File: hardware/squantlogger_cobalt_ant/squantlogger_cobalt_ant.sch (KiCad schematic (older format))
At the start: 5 parts, among them J1 JTAG_2X05, M1 SUPERTRONIC37_51, M2 LPC824M201JHI33

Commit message: * updated cobalt ant datalogger PCB
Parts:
- removed M1: SUPERTRONIC37_51, SquantorPcbOutline:SUPERTRONIC_PP40, symbol SUPERTRONIC37_51
- added H1: Drill_Hole_no_metal, SquantorPcbOutline:MountingHole_2.2mm_no_metal, symbol Drill_Hole_no_metal
- added H2, H3: Drill_Hole_no_metal, SquantorPcbOutline:MountingHole_3.0mm_no_metal, symbol Drill_Hole_no_metal
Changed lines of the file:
@@
 $EndComp
 $Comp
-L GND #PWR01
+L GND #PWR2
 U 1 1 5921F82A
 P 2950 2200
-F 0 "#PWR01" H 2950 1950 50  0001 C CNN
+F 0 "#PWR2" H 2950 1950 50  0001 C CNN
 F 1 "GND" H 2950 2050 50  0000 C CNN
 F 2 "" H 2950 2200 50  0001 C CNN
@@
 $EndComp
 $Comp
-L VCC #PWR02
+L VCC #PWR1
 U 1 1 5921F856
 P 2950 1700
-F 0 "#PWR02" H 2950 1550 50  0001 C CNN
+F 0 "#PWR1" H 2950 1550 50  0001 C CNN
 F 1 "VCC" H 2950 1850 50  0000 C CNN
 F 2 "" H 2950 1700 50  0001 C CNN
@@
 	1900 2150 1150 2150
 $Comp
-L SUPERTRONIC37_51 M1
-U 1 1 5921FBE6
-P 2100 3550
-F 0 "M1" H 1700 3450 45  0000 L BNN
-F 1 "SUPERTRONIC37_51" H 1700 3250 45  0000 L BNN
-F 2 "SquantorPcbOutline:SUPERTRONIC_PP40" H 2130 3700 20  0001 C CNN
-F 3 "" H 2100 3550 60  0001 C CNN
-	1    2100 3550
-	1    0    0    -1
-$EndComp
-$Comp
-L GND #PWR03
+L GND #PWR3
 U 1 1 5921FF75
 P 8100 4100
-F 0 "#PWR03" H 8100 3850 50  0001 C CNN
+F 0 "#PWR3" H 8100 3850 50  0001 C CNN
 F 1 "GND" H 8100 3950 50  0000 C CNN
 F 2 "" H 8100 4100 50  0001 C CNN
@@
 $EndComp
 $Comp
-L VCC #PWR04
+L VCC #PWR6
 U 1 1 5921FFB7
 P 8950 3550
-F 0 "#PWR04" H 8950 3400 50  0001 C CNN
+F 0 "#PWR6" H 8950 3400 50  0001 C CNN
 F 1 "VCC" H 8950 3700 50  0000 C CNN
 F 2 "" H 8950 3550 50  0001 C CNN
@@
 	8800 3550 8950 3550
 $Comp
-L GND #PWR05
+L GND #PWR5
 U 1 1 59220010
 P 8950 3450
-F 0 "#PWR05" H 8950 3200 50  0001 C CNN
+F 0 "#PWR5" H 8950 3200 50  0001 C CNN
 F 1 "GND" H 8950 3300 50  0000 C CNN
 F 2 "" H 8950 3450 50  0001 C CNN
@@
 	8800 3450 8950 3450
 $Comp
-L VCC #PWR06
+L VCC #PWR4
 U 1 1 59220055
 P 8950 3350
-F 0 "#PWR06" H 8950 3200 50  0001 C CNN
+F 0 "#PWR4" H 8950 3200 50  0001 C CNN
 F 1 "VCC" H 8950 3500 50  0000 C CNN
 F 2 "" H 8950 3350 50  0001 C CNN
@@
 	2900 1950 2950 1950
 Connection ~ 2950 1950
+$Comp
+L Drill_Hole_no_metal H1
+U 1 1 592DD359
+P 1700 6350
+F 0 "H1" H 1700 6100 60  0000 C CNN
+F 1 "Drill_Hole_no_metal" H 1700 6600 60  0000 C CNN
+F 2 "SquantorPcbOutline:MountingHole_2.2mm_no_metal" H 1700 6350 60  0000 C CNN
+F 3 "" H 1700 6350 60  0001 C CNN
+	1    1700 6350
+	1    0    0    -1
+$EndComp
+$Comp
+L Drill_Hole_no_metal H2
+U 1 1 592DD3BE
+P 1700 6950
+F 0 "H2" H 1700 6700 60  0000 C CNN
+F 1 "Drill_Hole_no_metal" H 1700 7200 60  0000 C CNN
+F 2 "SquantorPcbOutline:MountingHole_3.0mm_no_metal" H 1700 6950 60  0000 C CNN
+F 3 "" H 1700 6950 60  0001 C CNN
+	1    1700 6950
+	1    0    0    -1
+$EndComp
+$Comp
+L Drill_Hole_no_metal H3
+U 1 1 592DD415
+P 1700 7550
+F 0 "H3" H 1700 7300 60  0000 C CNN
+F 1 "Drill_Hole_no_metal" H 1700 7800 60  0000 C CNN
+F 2 "SquantorPcbOutline:MountingHole_3.0mm_no_metal" H 1700 7550 60  0000 C CNN
+F 3 "" H 1700 7550 60  0001 C CNN
+	1    1700 7550
+	1    0    0    -1
+$EndComp
 $EndSCHEMATC

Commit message: * some small mods
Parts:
- added J? (x2): PINS_1X12, symbol PINS_1X12
- added M1: SUPERTRONIC37_51, SquantorPcbOutline:SUPERTRONIC_PP40_logger, symbol SUPERTRONIC37_51
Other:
- moved on the sheet: J1, R1, R2
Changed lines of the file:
@@
 L JTAG_2X05 J1
 U 1 1 5921F65D
-P 2400 1950
-F 0 "J1" H 2400 2300 60  0000 C CNN
-F 1 "JTAG_2X05" H 2400 1600 60  0000 C CNN
-F 2 "SquantorConnectors:Header-0127-2X05-SMD" H 2400 2100 60  0001 C CNN
-F 3 "" H 2400 2100 60  0001 C CNN
-	1    2400 1950
+P 2250 1100
+F 0 "J1" H 2250 1450 60  0000 C CNN
+F 1 "JTAG_2X05" H 2250 750 60  0000 C CNN
+F 2 "SquantorConnectors:Header-0127-2X05-SMD" H 2250 1250 60  0001 C CNN
+F 3 "" H 2250 1250 60  0001 C CNN
+	1    2250 1100
 	1    0    0    -1
 $EndComp
@@
 L R R2
 U 1 1 5921F706
-P 1650 1750
-F 0 "R2" V 1730 1750 50  0000 C CNN
-F 1 "33" V 1650 1750 50  0000 C CNN
-F 2 "SquantorRcl:R_0402_hand" V 1580 1750 50  0001 C CNN
-F 3 "" H 1650 1750 50  0001 C CNN
-	1    1650 1750
+P 1500 900
+F 0 "R2" V 1580 900 50  0000 C CNN
+F 1 "33" V 1500 900 50  0000 C CNN
+F 2 "SquantorRcl:R_0402_hand" V 1430 900 50  0001 C CNN
+F 3 "" H 1500 900 50  0001 C CNN
+	1    1500 900
 	0    1    1    0
 $EndComp
@@
 L R R1
 U 1 1 5921F77B
-P 1400 1850
-F 0 "R1" V 1480 1850 50  0000 C CNN
-F 1 "33" V 1400 1850 50  0000 C CNN
-F 2 "SquantorRcl:R_0402_hand" V 1330 1850 50  0001 C CNN
-F 3 "" H 1400 1850 50  0001 C CNN
-	1    1400 1850
+P 1250 1000
+F 0 "R1" V 1330 1000 50  0000 C CNN
+F 1 "33" V 1250 1000 50  0000 C CNN
+F 2 "SquantorRcl:R_0402_hand" V 1180 1000 50  0001 C CNN
+F 3 "" H 1250 1000 50  0001 C CNN
+	1    1250 1000
 	0    1    1    0
 $EndComp
@@
 L GND #PWR2
 U 1 1 5921F82A
-P 2950 2200
-F 0 "#PWR2" H 2950 1950 50  0001 C CNN
-F 1 "GND" H 2950 2050 50  0000 C CNN
-F 2 "" H 2950 2200 50  0001 C CNN
-F 3 "" H 2950 2200 50  0001 C CNN
-	1    2950 2200
+P 2800 1350
+F 0 "#PWR2" H 2800 1100 50  0001 C CNN
+F 1 "GND" H 2800 1200 50  0000 C CNN
+F 2 "" H 2800 1350 50  0001 C CNN
+F 3 "" H 2800 1350 50  0001 C CNN
+	1    2800 1350
 	1    0    0    -1
 $EndComp
@@
 L VCC #PWR1
 U 1 1 5921F856
-P 2950 1700
-F 0 "#PWR1" H 2950 1550 50  0001 C CNN
-F 1 "VCC" H 2950 1850 50  0000 C CNN
-F 2 "" H 2950 1700 50  0001 C CNN
-F 3 "" H 2950 1700 50  0001 C CNN
-	1    2950 1700
-	1    0    0    -1
-$EndComp
-Wire Wire Line
-	2900 1750 2950 1750
-Wire Wire Line
-	2950 1750 2950 1700
-Wire Wire Line
-	2900 2150 2950 2150
-Wire Wire Line
-	2950 1850 2950 2200
-Wire Wire Line
-	1900 1750 1800 1750
-Wire Wire Line
-	1900 1850 1550 1850
-Text GLabel 1150 1750 0    60   Input ~ 0
+P 2800 850
+F 0 "#PWR1" H 2800 700 50  0001 C CNN
+F 1 "VCC" H 2800 1000 50  0000 C CNN
+F 2 "" H 2800 850 50  0001 C CNN
+F 3 "" H 2800 850 50  0001 C CNN
+	1    2800 850
+	1    0    0    -1
+$EndComp
+Wire Wire Line
+	2750 900  2800 900
+Wire Wire Line
+	2800 900  2800 850
+Wire Wire Line
+	2750 1300 2800 1300
+Wire Wire Line
+	2800 1000 2800 1350
+Wire Wire Line
+	1750 900  1650 900
+Wire Wire Line
+	1750 1000 1400 1000
+Text GLabel 1000 900  0    60   Input ~ 0
 SWDIO
-Text GLabel 1150 1850 0    60   Input ~ 0
+Text GLabel 1000 1000 0    60   Input ~ 0
 SWDCLK
 Wire Wire Line
-	1500 1750 1150 1750
-Wire Wire Line
-	1250 1850 1150 1850
-Text GLabel 1150 2150 0    60   Input ~ 0
+	1350 900  1000 900
+Wire Wire Line
+	1100 1000 1000 1000
+Text GLabel 1000 1300 0    60   Input ~ 0
 nRESET
 Wire Wire Line
-	1900 2150 1150 2150
+	1750 1300 1000 1300
 $Comp
 L GND #PWR3
@@
 	7400 2650 7300 2650
 Wire Wire Line
-	2900 1850 2950 1850
-Connection ~ 2950 2150
-Wire Wire Line
-	2900 1950 2950 1950
-Connection ~ 2950 1950
+	2750 1000 2800 1000
+Connection ~ 2800 1300
+Wire Wire Line
+	2750 1100 2800 1100
+Connection ~ 2800 1100
 $Comp
 L Drill_Hole_no_metal H1
@@
 	1    0    0    -1
 $EndComp
+$Comp
+L SUPERTRONIC37_51 M1
+U 1 1 59386C4C
+P 4050 6750
+F 0 "M1" H 3650 6650 45  0000 L BNN
+F 1 "SUPERTRONIC37_51" H 3650 6450 45  0000 L BNN
+F 2 "SquantorPcbOutline:SUPERTRONIC_PP40_logger" H 4080 6900 20  0000 C CNN
+F 3 "" H 4050 6750 60  0001 C CNN
+	1    4050 6750
+	1    0    0    -1
+$EndComp
+$Comp
+L PINS_1X12 J?
+U 1 1 59386E63
+P 750 2300
+F 0 "J?" H 700 3000 60  0000 C CNN
+F 1 "PINS_1X12" H 750 1600 60  0000 C CNN
+F 2 "" H 750 2850 60  0001 C CNN
+F 3 "" H 750 2850 60  0001 C CNN
+	1    750  2300
+	1    0    0    -1
+$EndComp
+$Comp
+L PINS_1X12 J?
+U 1 1 59386ED0
+P 750 3800
+F 0 "J?" H 700 4500 60  0000 C CNN
+F 1 "PINS_1X12" H 750 3100 60  0000 C CNN
+F 2 "" H 750 4350 60  0001 C CNN
+F 3 "" H 750 4350 60  0001 C CNN
+	1    750  3800
+	1    0    0    -1
+$EndComp

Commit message: * added few tidbits
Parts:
- added C? (x2): 10u, SquantorRcl:C_0805, symbol C
- H2, H3: footprint SquantorPcbOutline:MountingHole_3.0mm_no_metal -> SquantorPcbOutline:MountingHole_3.2mm_no_metal
- gave numbers to parts that had none: 2
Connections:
- net labels added: GNDA, VDD, VDDA
- wire segments 18 -> 22
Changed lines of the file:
@@
 LIBS:contrib
 LIBS:valves
+LIBS:SquantorPCBOutline
+LIBS:SquantorRCL
+LIBS:SquantorConnectors
 LIBS:SquantorButtons
-LIBS:SquantorConnectors
 LIBS:SquantorNxp
-LIBS:SquantorUsb
-LIBS:SquantorWinbond
-LIBS:SquantorAtmel
-LIBS:SquantorPCBOutline
 LIBS:squantlogger_cobalt_ant-cache
 EELAYER 25 0
@@
 $EndComp
 $Comp
-L GND #PWR2
+L GND #PWR6
 U 1 1 5921F82A
 P 2800 1350
-F 0 "#PWR2" H 2800 1100 50  0001 C CNN
+F 0 "#PWR6" H 2800 1100 50  0001 C CNN
 F 1 "GND" H 2800 1200 50  0000 C CNN
 F 2 "" H 2800 1350 50  0001 C CNN
@@
 $EndComp
 $Comp
-L VCC #PWR1
+L VCC #PWR5
 U 1 1 5921F856
 P 2800 850
-F 0 "#PWR1" H 2800 700 50  0001 C CNN
+F 0 "#PWR5" H 2800 700 50  0001 C CNN
 F 1 "VCC" H 2800 1000 50  0000 C CNN
 F 2 "" H 2800 850 50  0001 C CNN
@@
 	1750 1300 1000 1300
 $Comp
-L GND #PWR3
+L GND #PWR7
 U 1 1 5921FF75
 P 8100 4100
-F 0 "#PWR3" H 8100 3850 50  0001 C CNN
+F 0 "#PWR7" H 8100 3850 50  0001 C CNN
 F 1 "GND" H 8100 3950 50  0000 C CNN
 F 2 "" H 8100 4100 50  0001 C CNN
@@
 	1    0    0    -1
 $EndComp
-$Comp
-L VCC #PWR6
-U 1 1 5921FFB7
-P 8950 3550
-F 0 "#PWR6" H 8950 3400 50  0001 C CNN
-F 1 "VCC" H 8950 3700 50  0000 C CNN
-F 2 "" H 8950 3550 50  0001 C CNN
-F 3 "" H 8950 3550 50  0001 C CNN
-	1    8950 3550
-	0    1    1    0
-$EndComp
 Wire Wire Line
 	8100 4100 8100 3950
 Wire Wire Line
 	8800 3550 8950 3550
-$Comp
-L GND #PWR5
-U 1 1 59220010
-P 8950 3450
-F 0 "#PWR5" H 8950 3200 50  0001 C CNN
-F 1 "GND" H 8950 3300 50  0000 C CNN
-F 2 "" H 8950 3450 50  0001 C CNN
-F 3 "" H 8950 3450 50  0001 C CNN
-	1    8950 3450
-	0    -1   -1   0
-$EndComp
 Wire Wire Line
 	8800 3450 8950 3450
-$Comp
-L VCC #PWR4
-U 1 1 59220055
-P 8950 3350
-F 0 "#PWR4" H 8950 3200 50  0001 C CNN
-F 1 "VCC" H 8950 3500 50  0000 C CNN
-F 2 "" H 8950 3350 50  0001 C CNN
-F 3 "" H 8950 3350 50  0001 C CNN
-	1    8950 3350
-	0    1    1    0
-$EndComp
 Wire Wire Line
 	8800 3350 8950 3350
@@
 F 0 "H2" H 1700 6700 60  0000 C CNN
 F 1 "Drill_Hole_no_metal" H 1700 7200 60  0000 C CNN
-F 2 "SquantorPcbOutline:MountingHole_3.0mm_no_metal" H 1700 6950 60  0000 C CNN
+F 2 "SquantorPcbOutline:MountingHole_3.2mm_no_metal" H 1700 6950 60  0000 C CNN
 F 3 "" H 1700 6950 60  0001 C CNN
 	1    1700 6950
@@
 F 0 "H3" H 1700 7300 60  0000 C CNN
 F 1 "Drill_Hole_no_metal" H 1700 7800 60  0000 C CNN
-F 2 "SquantorPcbOutline:MountingHole_3.0mm_no_metal" H 1700 7550 60  0000 C CNN
+F 2 "SquantorPcbOutline:MountingHole_3.2mm_no_metal" H 1700 7550 60  0000 C CNN
 F 3 "" H 1700 7550 60  0001 C CNN
 	1    1700 7550
@@
 L SUPERTRONIC37_51 M1
 U 1 1 59386C4C
-P 4050 6750
-F 0 "M1" H 3650 6650 45  0000 L BNN
-F 1 "SUPERTRONIC37_51" H 3650 6450 45  0000 L BNN
-F 2 "SquantorPcbOutline:SUPERTRONIC_PP40_logger" H 4080 6900 20  0000 C CNN
-F 3 "" H 4050 6750 60  0001 C CNN
-	1    4050 6750
-	1    0    0    -1
-$EndComp
-$Comp
-L PINS_1X12 J?
+P 6200 7150
+F 0 "M1" H 5800 7050 45  0000 L BNN
+F 1 "SUPERTRONIC37_51" H 5800 6850 45  0000 L BNN
+F 2 "SquantorPcbOutline:SUPERTRONIC_PP40_logger" H 6230 7300 20  0000 C CNN
+F 3 "" H 6200 7150 60  0001 C CNN
+	1    6200 7150
+	1    0    0    -1
+$EndComp
+$Comp
+L PINS_1X12 J2
 U 1 1 59386E63
 P 750 2300
-F 0 "J?" H 700 3000 60  0000 C CNN
+F 0 "J2" H 700 3000 60  0000 C CNN
 F 1 "PINS_1X12" H 750 1600 60  0000 C CNN
 F 2 "" H 750 2850 60  0001 C CNN
@@
 $EndComp
 $Comp
-L PINS_1X12 J?
+L PINS_1X12 J3
 U 1 1 59386ED0
 P 750 3800
-F 0 "J?" H 700 4500 60  0000 C CNN
+F 0 "J3" H 700 4500 60  0000 C CNN
 F 1 "PINS_1X12" H 750 3100 60  0000 C CNN
 F 2 "" H 750 4350 60  0001 C CNN
@@
 	1    0    0    -1
 $EndComp
+$Comp
+L GNDA #PWR2
+U 1 1 5939A617
+P 800 5350
+F 0 "#PWR2" H 800 5100 50  0001 C CNN
+F 1 "GNDA" H 800 5200 50  0000 C CNN
+F 2 "" H 800 5350 50  0001 C CNN
+F 3 "" H 800 5350 50  0001 C CNN
+	1    800  5350
+	1    0    0    -1
+$EndComp
+$Comp
+L GND #PWR4
+U 1 1 5939A647
+P 1050 5350
+F 0 "#PWR4" H 1050 5100 50  0001 C CNN
+F 1 "GND" H 1050 5200 50  0000 C CNN
+F 2 "" H 1050 5350 50  0001 C CNN
+F 3 "" H 1050 5350 50  0001 C CNN
+	1    1050 5350
+	1    0    0    -1
+$EndComp
+$Comp
+L GNDA #PWR9
+U 1 1 5939A7EA
+P 8950 3450
+F 0 "#PWR9" H 8950 3200 50  0001 C CNN
+F 1 "GNDA" H 8950 3300 50  0000 C CNN
+F 2 "" H 8950 3450 50  0001 C CNN
+F 3 "" H 8950 3450 50  0001 C CNN
+	1    8950 3450
+	0    -1   -1   0
+$EndComp
+$Comp
+L VDD #PWR10
+U 1 1 5939A870
+P 8950 3550
+F 0 "#PWR10" H 8950 3400 50  0001 C CNN
+F 1 "VDD" H 8950 3700 50  0000 C CNN
+F 2 "" H 8950 3550 50  0001 C CNN
+F 3 "" H 8950 3550 50  0001 C CNN
+	1    8950 3550
+	0    1    1    0
+$EndComp
+$Comp
+L VDDA #PWR8
+U 1 1 5939A898
+P 8950 3350
+F 0 "#PWR8" H 8950 3200 50  0001 C CNN
+F 1 "VDDA" H 8950 3500 50  0000 C CNN
+F 2 "" H 8950 3350 50  0001 C CNN
+F 3 "" H 8950 3350 50  0001 C CNN
+	1    8950 3350
+	0    1    1    0
+$EndComp
+$Comp
+L VDD #PWR3
+U 1 1 5939AA02
+P 1050 4950
+F 0 "#PWR3" H 1050 4800 50  0001 C CNN
+F 1 "VDD" H 1050 5100 50  0000 C CNN
+F 2 "" H 1050 4950 50  0001 C CNN
+F 3 "" H 1050 4950 50  0001 C CNN
+	1    1050 4950
+	1    0    0    -1
+$EndComp
+$Comp
+L VDDA #PWR1
+U 1 1 5939AA2B
+P 800 4950
+F 0 "#PWR1" H 800 4800 50  0001 C CNN
+F 1 "VDDA" H 800 5100 50  0000 C CNN
+F 2 "" H 800 4950 50  0001 C CNN
+F 3 "" H 800 4950 50  0001 C CNN
+	1    800  4950
+	1    0    0    -1
+$EndComp
+$Comp
+L C C?
+U 1 1 5939A5DB
+P 800 5150
+F 0 "C?" H 825 5250 50  0000 L CNN
+F 1 "10u" H 825 5050 50  0000 L CNN
+F 2 "SquantorRcl:C_0805" H 838 5000 50  0001 C CNN
+F 3 "" H 800 5150 50  0001 C CNN
+	1    800  5150
+	1    0    0    -1
+$EndComp
+$Comp
+L C C?
+U 1 1 5939A905
+P 1050 5150
+F 0 "C?" H 1075 5250 50  0000 L CNN
+F 1 "10u" H 1075 5050 50  0000 L CNN
+F 2 "SquantorRcl:C_0805" H 1088 5000 50  0001 C CNN
+F 3 "" H 1050 5150 50  0001 C CNN
+	1    1050 5150
+	1    0    0    -1
+$EndComp
+Wire Wire Line
+	800  5000 800  4950
+Wire Wire Line
+	800  5300 800  5350
+Wire Wire Line
+	1050 5350 1050 5300
+Wire Wire Line
+	1050 5000 1050 4950
 $EndSCHEMATC

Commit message: * some further work on the cobalt ant datalogger
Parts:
- removed M1: SUPERTRONIC37_51, SquantorPcbOutline:SUPERTRONIC_PP40_logger, symbol SUPERTRONIC37_51
- removed M2: LPC824M201JHI33, SquantorNxp:SOT617-3, symbol LPC824M201JHI33
- added C3: 1u, SquantorRcl:C_0805, symbol C
- added C4, C6: 10n, SquantorRcl:C_0402, symbol C
- added C5, C7: 1u, SquantorRcl:C_0402, symbol C
- added J4: PINS_1X06, SquantorConnectors:Header-0254-1X06-H010, symbol PINS_1X06
- added M1: LPC824M201JDH20, SquantorNxp:SOT360, symbol LPC824M201JDH20
- added R3, R4, R5, R6: 100, SquantorRcl:R_0402_hand, symbol R
- added R7, R8: 10k, SquantorRcl:R_0402_hand, symbol R
- added U1: MCP1702-MB, SquantorMicrochip:MB-(SOT-89), symbol MCP1702-MB
- J2, J3: footprint (none) -> SquantorConnectors:Header-0254-1X12-H010
- gave numbers to parts that had none: 2
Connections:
- net labels added: +BATT, SERIAL_CTS, SERIAL_RTS, SERIAL_RXD, SERIAL_TXD
- net labels removed: VCC
- wire segments 22 -> 52
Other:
- moved on the sheet: C1, C2

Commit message: * started fleshing out the schematic of the squantlogger
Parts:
- removed J4: PINS_1X06, SquantorConnectors:Header-0254-1X06-H010, symbol PINS_1X06
- removed M1: LPC824M201JDH20, SquantorNxp:SOT360, symbol LPC824M201JDH20
- added 2.2k (x2): R, SquantorRcl:R_0402_hand, symbol R
- added J?: FTDI_PINS_1X06, symbol FTDI_PINS_1X06
- added M?: LPC824M201JHI33, SquantorNxp_SOT617-3, symbol LPC824M201JHI33
- added R? (x2): OPT, symbol R
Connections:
- net labels added: ADC_0, ADC_1, ADC_2, ADC_3, ADC_4, ADC_5, ADC_6, ADC_7, ADC_8, I2C_SCL, I2C_SDA, VREF
- wire segments 52 -> 82
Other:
- moved on the sheet: C4, C5, C6, C7

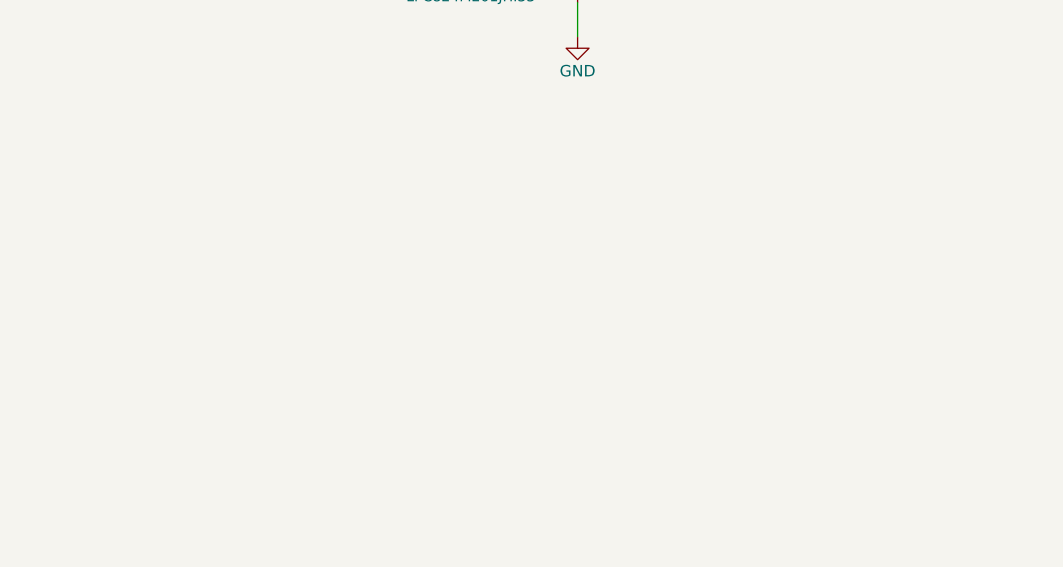
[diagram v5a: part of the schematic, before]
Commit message: * added spi flash to schematic
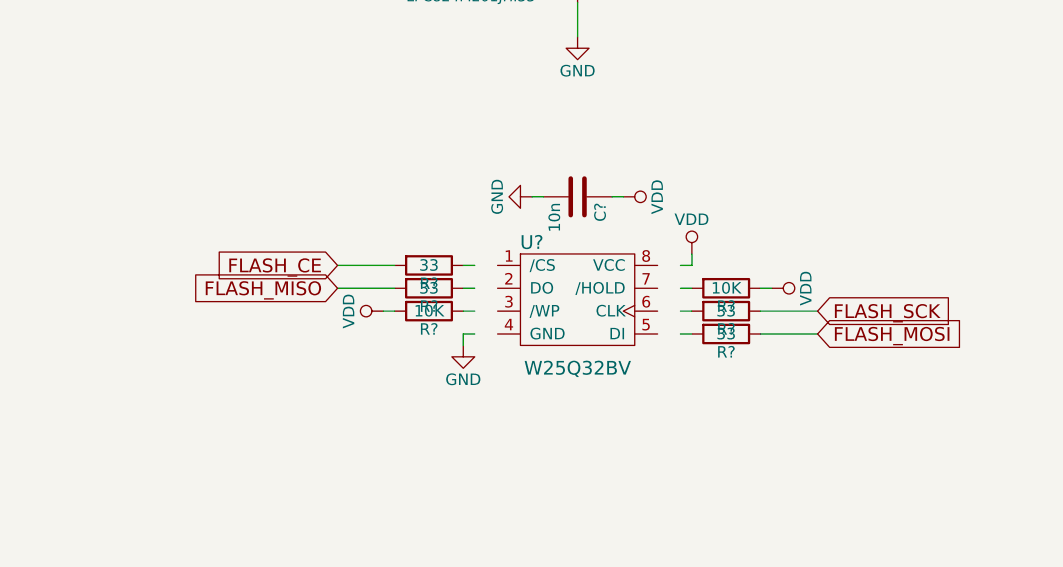
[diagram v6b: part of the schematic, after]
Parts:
- added C?: 10n, SquantorRcl:C_0402, symbol C
- added R? (x4): 33, SquantorRcl:R_0402_hand, symbol R
- added R? (x2): 10K, SquantorRcl:R_0402_hand, symbol R
- added U?: W25Q32BV, symbol W25Q32BV
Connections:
- net labels added: FLASH_CE, FLASH_MISO, FLASH_MOSI, FLASH_SCK
- wire segments 82 -> 100
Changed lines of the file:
@@
 LIBS:SquantorNxp
 LIBS:SquantorMicrochip
+LIBS:SquantorWinbond
 LIBS:squantlogger_cobalt_ant-cache
 EELAYER 25 0
@@
 Wire Wire Line
 	1000 4350 950  4350
+$Comp
+L W25Q32BV U?
+U 1 1 595545DA
+P 9200 4550
+F 0 "U?" H 9000 4800 60  0000 C CNN
+F 1 "W25Q32BV" H 9200 4250 60  0000 C CNN
+F 2 "" H 9150 4550 60  0001 C CNN
+F 3 "" H 9150 4550 60  0001 C CNN
+	1    9200 4550
+	1    0    0    -1
+$EndComp
+Text GLabel 8150 4400 0    60   Input ~ 0
+FLASH_CE
+$Comp
+L R R?
+U 1 1 59554929
+P 8550 4400
+F 0 "R?" V 8630 4400 50  0000 C CNN
+F 1 "33" V 8550 4400 50  0000 C CNN
+F 2 "SquantorRcl:R_0402_hand" V 8480 4400 50  0001 C CNN
+F 3 "" H 8550 4400 50  0001 C CNN
+	1    8550 4400
+	0    1    1    0
+$EndComp
+$Comp
+L R R?
+U 1 1 5955498E
+P 8550 4500
+F 0 "R?" V 8630 4500 50  0000 C CNN
+F 1 "33" V 8550 4500 50  0000 C CNN
+F 2 "SquantorRcl:R_0402_hand" V 8480 4500 50  0001 C CNN
+F 3 "" H 8550 4500 50  0001 C CNN
+	1    8550 4500
+	0    1    1    0
+$EndComp
+$Comp
+L R R?
+U 1 1 595549FD
+P 8550 4600
+F 0 "R?" V 8630 4600 50  0000 C CNN
+F 1 "10K" V 8550 4600 50  0000 C CNN
+F 2 "SquantorRcl:R_0402_hand" V 8480 4600 50  0001 C CNN
+F 3 "" H 8550 4600 50  0001 C CNN
+	1    8550 4600
+	0    1    1    0
+$EndComp
+$Comp
+L GND #PWR?
+U 1 1 59554BC2
+P 8700 4750
+F 0 "#PWR?" H 8700 4500 50  0001 C CNN
+F 1 "GND" H 8700 4600 50  0000 C CNN
+F 2 "" H 8700 4750 50  0001 C CNN
+F 3 "" H 8700 4750 50  0001 C CNN
+	1    8700 4750
+	1    0    0    -1
+$EndComp
+$Comp
+L VDD #PWR?
+U 1 1 59554E4D
+P 9700 4350
+F 0 "#PWR?" H 9700 4200 50  0001 C CNN
+F 1 "VDD" H 9700 4500 50  0000 C CNN
+F 2 "" H 9700 4350 50  0001 C CNN
+F 3 "" H 9700 4350 50  0001 C CNN
+	1    9700 4350
+	1    0    0    -1
+$EndComp
+Wire Wire Line
+	8700 4750 8700 4700
+Wire Wire Line
+	8700 4700 8750 4700
+Wire Wire Line
+	9700 4350 9700 4400
+Wire Wire Line
+	9700 4400 9650 4400
+$Comp
+L R R?
+U 1 1 59555150
+P 9850 4500
+F 0 "R?" V 9930 4500 50  0000 C CNN
+F 1 "10K" V 9850 4500 50  0000 C CNN
+F 2 "SquantorRcl:R_0402_hand" V 9780 4500 50  0001 C CNN
+F 3 "" H 9850 4500 50  0001 C CNN
+	1    9850 4500
+	0    1    1    0
+$EndComp
+$Comp
+L R R?
+U 1 1 595551BF
+P 9850 4600
+F 0 "R?" V 9930 4600 50  0000 C CNN
+F 1 "33" V 9850 4600 50  0000 C CNN
+F 2 "SquantorRcl:R_0402_hand" V 9780 4600 50  0001 C CNN
+F 3 "" H 9850 4600 50  0001 C CNN
+	1    9850 4600
+	0    1    1    0
+$EndComp
+$Comp
+L R R?
+U 1 1 5955521E
+P 9850 4700
+F 0 "R?" V 9930 4700 50  0000 C CNN
+F 1 "33" V 9850 4700 50  0000 C CNN
+F 2 "SquantorRcl:R_0402_hand" V 9780 4700 50  0001 C CNN
+F 3 "" H 9850 4700 50  0001 C CNN
+	1    9850 4700
+	0    1    1    0
+$EndComp
+$Comp
+L VDD #PWR?
+U 1 1 5955531A
+P 10050 4500
+F 0 "#PWR?" H 10050 4350 50  0001 C CNN
+F 1 "VDD" H 10050 4650 50  0000 C CNN
+F 2 "" H 10050 4500 50  0001 C CNN
+F 3 "" H 10050 4500 50  0001 C CNN
+	1    10050 4500
+	0    1    1    0
+$EndComp
+Wire Wire Line
+	9650 4500 9700 4500
+Wire Wire Line
+	10000 4500 10050 4500
+Wire Wire Line
+	8750 4400 8700 4400
+Wire Wire Line
+	8400 4400 8150 4400
+Text GLabel 8150 4500 0    60   Input ~ 0
+FLASH_MISO
+$Comp
+L VDD #PWR?
+U 1 1 5955568A
+P 8350 4600
+F 0 "#PWR?" H 8350 4450 50  0001 C CNN
+F 1 "VDD" H 8350 4750 50  0000 C CNN
+F 2 "" H 8350 4600 50  0001 C CNN
+F 3 "" H 8350 4600 50  0001 C CNN
+	1    8350 4600
+	0    -1   -1   0
+$EndComp
+Wire Wire Line
+	8400 4600 8350 4600
+Wire Wire Line
+	8150 4500 8400 4500
+Wire Wire Line
+	8700 4500 8750 4500
+Wire Wire Line
+	8750 4600 8700 4600
+Text GLabel 10250 4600 2    60   Input ~ 0
+FLASH_SCK
+Wire Wire Line
+	10250 4600 10000 4600
+Text GLabel 10250 4700 2    60   Input ~ 0
+FLASH_MOSI
+Wire Wire Line
+	9650 4600 9700 4600
+Wire Wire Line
+	10000 4700 10250 4700
+Wire Wire Line
+	9700 4700 9650 4700
+$Comp
+L C C?
+U 1 1 595562F6
+P 9200 4100
+F 0 "C?" H 9225 4200 50  0000 L CNN
+F 1 "10n" H 9225 4000 50  0000 L CNN
+F 2 "SquantorRcl:C_0402" H 9238 3950 50  0001 C CNN
+F 3 "" H 9200 4100 50  0001 C CNN
+	1    9200 4100
+	0    1    1    0
+$EndComp
+$Comp
+L VDD #PWR?
+U 1 1 5955644C
+P 9400 4100
+F 0 "#PWR?" H 9400 3950 50  0001 C CNN
+F 1 "VDD" H 9400 4250 50  0000 C CNN
+F 2 "" H 9400 4100 50  0001 C CNN
+F 3 "" H 9400 4100 50  0001 C CNN
+	1    9400 4100
+	0    1    1    0
+$EndComp
+$Comp
+L GND #PWR?
+U 1 1 595564E7
+P 9000 4100
+F 0 "#PWR?" H 9000 3850 50  0001 C CNN
+F 1 "GND" H 9000 3950 50  0000 C CNN
+F 2 "" H 9000 4100 50  0001 C CNN
+F 3 "" H 9000 4100 50  0001 C CNN
+	1    9000 4100
+	0    1    1    0
+$EndComp
+Wire Wire Line
+	9400 4100 9350 4100
+Wire Wire Line
+	9050 4100 9000 4100
 $EndSCHEMATC
